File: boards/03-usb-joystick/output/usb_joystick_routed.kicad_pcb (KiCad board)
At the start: 2 copper layers, 80 x 60 mm, 19 parts, among them J1 USB-C, J2 Joystick, SW1 Button, SW2 Button, SW3 Button, SW4 Button, U1 MCU, Y1 16MHz

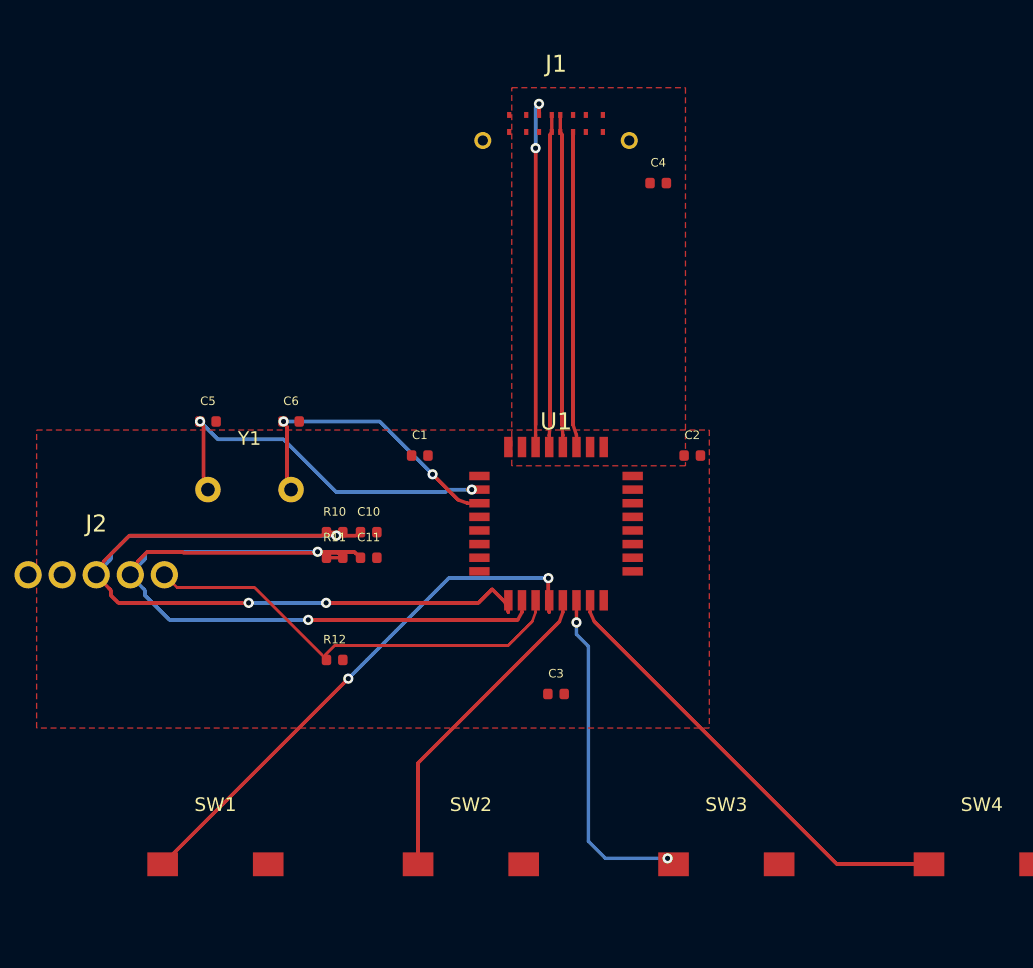
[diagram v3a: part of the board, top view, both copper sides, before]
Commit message: fix(router): grid re-marking after mutating optimizer passes (closes #3507) (#3510)
* fix(router): grid re-marking after mutating optimizer/nudge passes (#3507)

Post-route passes mutated route geometry without re-marking the routing
grid, so their own collision checking and every downstream grid consumer
(targeted repair re-routes, future nets) ran against stale copper:

- RoutingGrid.resync_route_occupancy: explicit resync API taking
  (stale, current) pairs -- unmarks pre-mutation cells (Python + C++
  mirror), swaps grid.routes bookkeeping, rebuilds both R-trees
  wholesale (in-place mutation invalidates id/envelope-keyed entries),
  re-marks all routes of affected nets, invalidates the C++
  stored-route snapshot.  Geometry-unchanged pairs are skipped
  (incremental unmark-old/mark-new perf shape).
- Route.copy_geometry: field-level geometry snapshots for in-place
  mutating passes.
- optimize_routes_grid_synced: grid-transactional optimizer loop
  (unmark old / mark new per mutated route) used by all four kct-route
  call sites and the board 06 recipe.
- drc_verify_and_nudge: snapshots geometry at entry and resyncs the
  grid on every exit path (including exceptions).
- enforce_connectivity_invariant: revert path now resyncs the grid
  with the restored pre-phase routes.
- boards/03: --raw dropped from the production recipe (and the pinned
  baseline-test invocation) -- the grid-transactional optimize retires
  the deterministic XTAL1/XTAL2 clearance_segment_via merge violation
  (closes-#3454 evidence: 13/13 nets + 0 DRC at jlcpcb-tier1 with the
  optimizer ON, seed 42, sidecar-aware check).

Co-Authored-By: Claude Opus 4.7 <noreply@anthropic.com>

* chore(boards): refresh board 03/06 artifacts under grid-synced passes; tighten board 06 floor 33 -> 20 (#3507)

Board 06 (seed 42, PYTHONHASHSEED=0): the 17-error USB3_RX1+/RX1-
overlap cluster (7 diffpair_clearance_intra + 10 clearance_segment_via)
is RETIRED -- the grid-transactional optimizer/nudge passes neve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
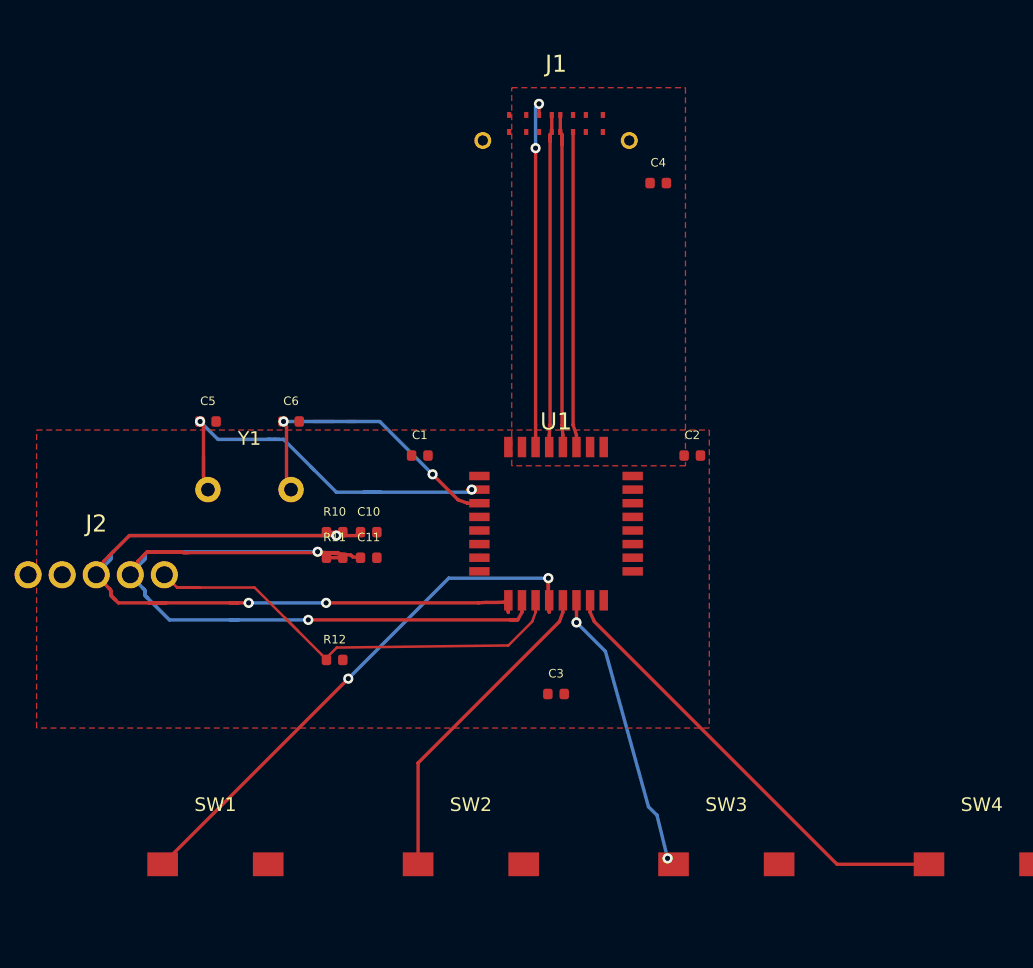
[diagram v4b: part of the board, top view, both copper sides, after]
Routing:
- net BTN3: track 20.0 -> 17.0 mm
- net JOY_X: track 59.2 -> 58.6 mm

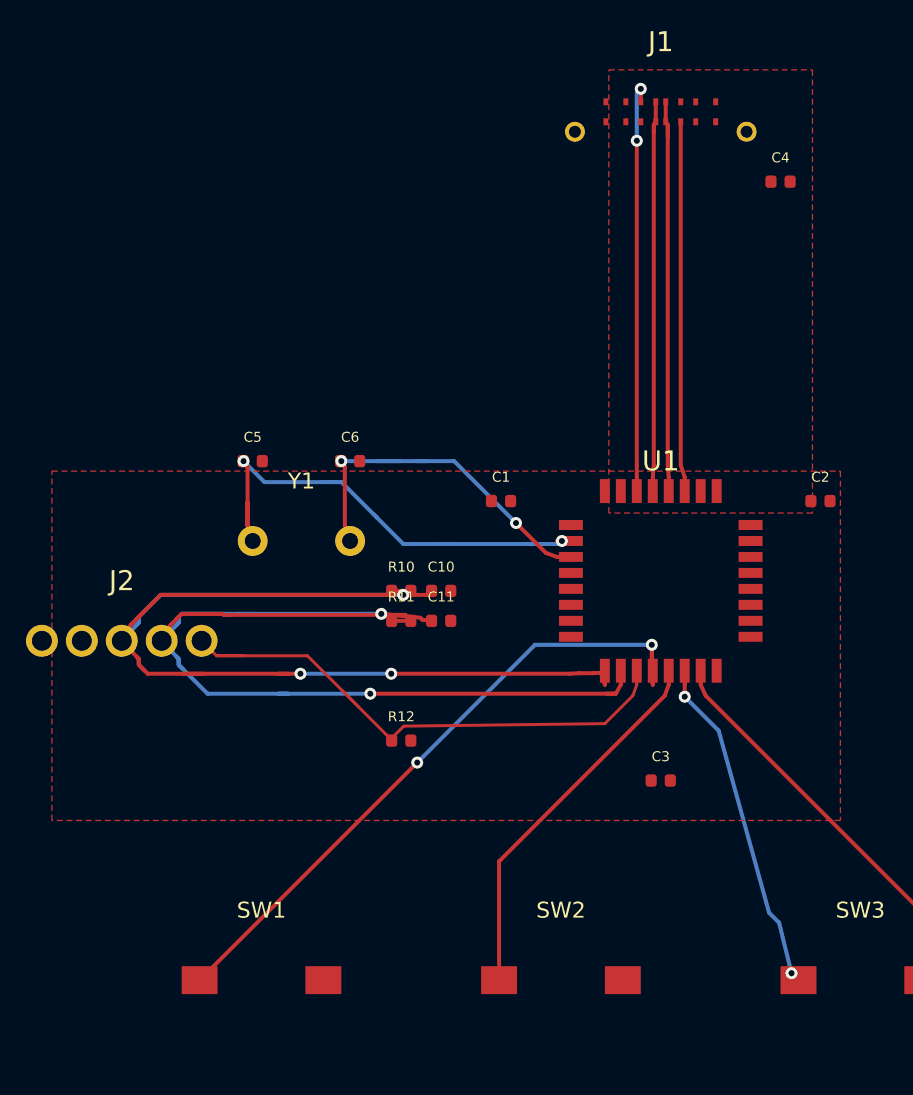
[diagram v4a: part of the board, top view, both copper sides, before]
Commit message: fix(router): 45° quantization in post-route mutation passes (closes #3532)
204/4519 segments on softstart's committed routed artifact sat 0.8-22.5°
off the 0/45/90/135 set; every fleet board carried the same class
(board 07: 297/909). Attribution: 127 pad-tail emissions (the C++
reconstruct_path / Python _convert_path_to_route connect the last grid
cell to the exact off-grid pad centre with one skewed segment), 41
step-10c/d repair chain drags (regex endpoint dragging in
generate_design.py), 36 optimizer mutations (pull-tight neighbour
re-aiming, chamfer terminal restoration).

Fixes at source, all sharing the new router/quantize.py helpers
(is_45_aligned / snap_direction_8 / dogleg_points / quantize_pcb_file):

* cpp_backend._convert_result_to_route splits skewed C++ tails into
  exact float64 doglegs (C++ float32 ulp is too coarse for exact legs)
* Python Router._convert_path_to_route emits dogleg pad tails; the
  extend-to-pad branch requires the extended segment to stay aligned
* convert_corners_45 terminal restoration emits doglegs, not skews
* pull_tight_pass declines windows whose neighbours are not parallel
  to the translation direction (the classic H-V-H jog still compresses)
* drc_nudge segment/via chain snaps decline drags that would skew an
  abutting segment off the 45° set
* softstart recipe: step-10c via slides snap to the 8-direction set;
  new step-10e runs quantize_pcb_file before the DRC gate

Committed artifacts repaired in place with the exact-decimal
quantize_pcb_file (dogleg endpoints preserved bit-for-bit, second-leg
uuids deterministic uuid5). Fleet census ratchet in
tests/test_fleet_45_census.py: softstart + boards 01-05 at 0 off-angle;
documented residuals (issue #3535) are 2 corridor chords where both
dogleg variants collide (06/07) and board 07's 55 DDR_DATA_BYTE_0
length-tuning meanders (doglegging breaks the exactly-tuned
match_group_length_skew).

DRC: softstart 0 violations at jlcpcb-tier1 (strict gate; manufacturers
override added 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
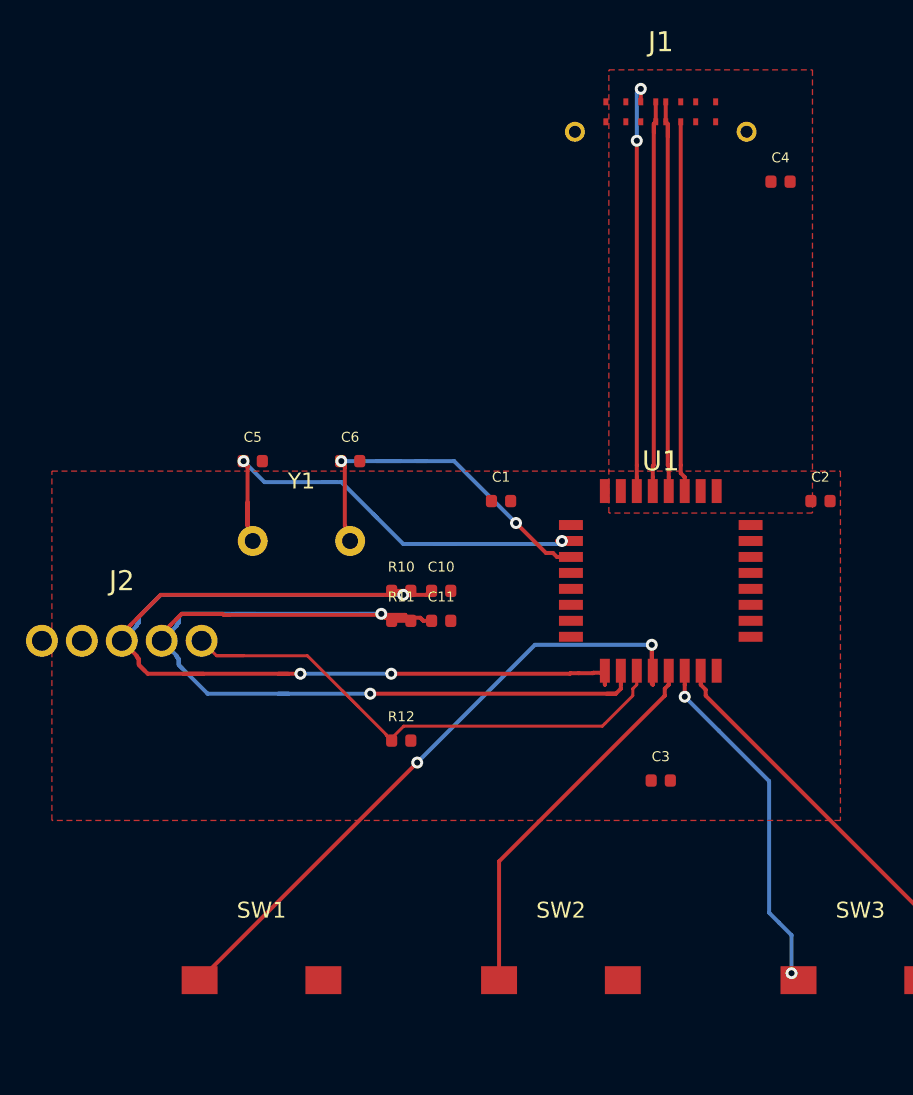
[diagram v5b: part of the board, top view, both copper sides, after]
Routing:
- net BTN3: track 17.0 -> 17.9 mm
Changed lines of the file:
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@@
 	(segment
 		(start 139.65 126.2)
+		(end 139.6 126.25)
+		(width 0.2)
+		(layer "F.Cu")
+		(net 4)
+	)
+	(segment
+		(start 139.6 126.25)
 		(end 139.6 126.8)
 		(width 0.2)
@@
 	(segment
 		(start 139.75 109)
+		(end 139.65 109.1)
+		(width 0.2)
+		(layer "F.Cu")
+		(net 4)
+	)
+	(segment
+		(start 139.65 109.1)
 		(end 139.65 109.15)
 		(width 0.2)
@@
 	(segment
 		(start 140.35 126.2)
+		(end 140.4 126.25)
+		(width 0.2)
+		(layer "F.Cu")
+		(net 5)
+	)
+	(segment
+		(start 140.4 126.25)
 		(end 140.4 126.8)
 		(width 0.2)
@@
 	(segment
 		(start 140.25 109)
+		(end 140.35 109.1)
+		(width 0.2)
+		(layer "F.Cu")
+		(net 5)
+	)
+	(segment
+		(start 140.35 109.1)
 		(end 140.35 109.15)
 		(width 0.2)
@@
 	(segment
 		(start 141.2 126.8)
+		(end 141 126.6)
+		(width 0.2)
+		(layer "F.Cu")
+		(net 7)
+	)
+	(segment
+		(start 141 126.6)
 		(end 141 126.2)
 		(width 0.2)
@@
 	(segment
 		(start 113.45 134.2)
+		(end 113 134.65)
+		(width 0.2)
+		(layer "F.Cu")
+		(net 8)
+	)
+	(segment
+		(start 113 134.65)
 		(end 113 135)
 		(width 0.2)
@@
 	(segment
 		(start 137 136.6)
+		(end 137.2 136.8)
+		(width 0.2)
+		(layer "F.Cu")
+		(net 8)
+	)
+	(segment
+		(start 137.2 136.8)
 		(end 137.2 137.2)
 		(width 0.2)
@@
 	(segment
 		(start 113 135)
+		(end 113.75 135.75)
+		(width 0.2)
+		(layer "F.Cu")
+		(net 8)
+	)
+	(segment
+		(start 113.75 135.75)
 		(end 113.75 135.8)
 		(width 0.2)
@@
 	(segment
 		(start 136.6036 136.6238)
+		(end 136.6274 136.6)
+		(width 0.2)
+		(layer "F.Cu")
+		(net 8)
+	)
+	(segment
+		(start 136.6274 136.6)
 		(end 137 136.6)
 		(width 0.2)
@@
 	(segment
 		(start 135.45 136.65)
+		(end 135.4763 136.6237)
+		(width 0.2)
+		(layer "F.Cu")
+		(net 8)
+	)
+	(segment
+		(start 135.4763 136.6237)
 		(end 135.8964 136.6237)
 		(width 0.2)
@@
 	(segment
 		(start 126.52 132.5)
+		(end 126.32 132.7)
+		(width 0.2)
+		(layer "F.Cu")
+		(net 8)
+	)
+	(segment
+		(start 126.32 132.7)
 		(end 126.25 132.7)
 		(width 0.2)
@@
 	(segment
 		(start 128.25 132.7)
+		(end 128.45 132.5)
+		(width 0.2)
+		(layer "F.Cu")
+		(net 8)
+	)
+	(segment
+		(start 128.45 132.5)
 		(end 128.52 132.5)
 		(width 0.2)
@@
 	(segment
 		(start 113 135)
+		(end 113.75 134.25)
+		(width 0.2)
+		(layer "B.Cu")
+		(net 8)
+	)
+	(segment
+		(start 113.75 134.25)
 		(end 113.75 134.2)
 		(width 0.2)
@@
 	(segment
 		(start 126 133.65)
+		(end 126.1947 133.8447)
+		(width 0.2)
+		(layer "F.Cu")
+		(net 9)
+	)
+	(segment
+		(start 126.1947 133.8447)
 		(end 127.9553 133.8447)
 		(width 0.2)
@@
 	(segment
 		(start 128.0553 133.9447)
+		(end 128.1106 134)
+		(width 0.2)
+		(layer "F.Cu")
+		(net 9)
+	)
+	(segment
+		(start 128.1106 134)
 		(end 128.52 134)
 		(width 0.2)
@@
 	(segment
 		(start 127.48 134)
+		(end 127.2 133.72)
+		(width 0.2)
+		(layer "F.Cu")
+		(net 9)
+	)
+	(segment
+		(start 127.2 133.72)
 		(end 127.2 133.7)
 		(width 0.2)
@@
 	(segment
 		(start 115.45 134.2)
+		(end 115 134.65)
+		(width 0.2)
+		(layer "F.Cu")
+		(net 9)
+	)
+	(segment
+		(start 115 134.65)
 		(end 115 135)
 		(width 0.2)
@@
 	(segment
 		(start 137.75 137.65)
+		(end 138 137.4)
+		(width 0.2)
+		(layer "F.Cu")
+		(net 9)
+	)
+	(segment
+		(start 138 137.4)
 		(end 138 137.2)
 		(width 0.2)
@@
 	(segment
 		(start 115 135)
+		(end 115.75 134.25)
+		(width 0.2)
+		(layer "B.Cu")
+		(net 9)
+	)
+	(segment
+		(start 115.75 134.25)
 		(end 115.75 134.2)
 		(width 0.2)
@@
 	(segment
 		(start 115 135)
+		(end 115.75 135.75)
+		(width 0.2)
+		(layer "B.Cu")
+		(net 9)
+	)
+	(segment
+		(start 115.75 135.75)
 		(end 115.75 135.8)
 		(width 0.2)
@@
 	(segment
 		(start 126.52 140)
+		(end 126.25 139.73)
+		(width 0.15)
+		(layer "F.Cu")
+		(net 10)
+	)
+	(segment
+		(start 126.25 139.73)
 		(end 126.25 139.7)
 		(width 0.15)
@@
 	(segment
 		(start 137.2 139.15)
+		(end 137.075 139.275)
+		(width 0.15)
+		(layer "F.Cu")
+		(net 10)
+	)
+	(segment
+		(start 137.075 139.275)
 		(end 127.125 139.275)
 		(width 0.15)
@@
 	(segment
 		(start 138.8 137.2)
+		(end 138.6 137.4)
+		(width 0.15)
+		(layer "F.Cu")
+		(net 10)
+	)
+	(segment
+		(start 138.6 137.4)
 		(end 138.6 137.75)
 		(width 0.15)
@@
 	(segment
 		(start 126.575 139.825)
+		(end 126.52 139.88)
+		(width 0.15)
+		(layer "F.Cu")
+		(net 10)
+	)
+	(segment
+		(start 126.52 139.88)
 		(end 126.52 140)
 		(width 0.15)
@@
 	(segment
 		(start 139.6 137.2)
+		(end 139.55 137.15)
+		(width 0.2)
+		(layer "F.Cu")
+		(net 11)
+	)
+	(segment
+		(start 139.55 137.15)
 		(end 139.55 136.6)
 		(width 0.2)
@@
 	(segment
 		(start 140.4 137.2)
+		(end 140.2 137.4)
+		(width 0.2)
+		(layer "F.Cu")
+		(net 12)
+	)
+	(segment
+		(start 140.2 137.4)
 		(end 140.2 137.75)
 		(width 0.2)
@@
 	(segment
 		(start 145.9279 149.1221)
+		(end 146.55 149.7442)
+		(width 0.2)
+		(layer "B.Cu")
+		(net 13)
+	)
+	(segment
+		(start 146.55 149.7442)
 		(end 146.55 151.65)
 		(width 0.2)
@@
 	(segment
 		(start 142.9 139.5)
+		(end 145.4279 142.0279)
+		(width 0.2)
+		(layer "B.Cu")
+		(net 13)
+	)
+	(segment
+		(start 145.4279 142.0279)
 		(end 145.4279 148.6221)
 		(width 0.2)
@@
 	(segment
 		(start 142 137.2)
+		(end 142.25 137.45)
+		(width 0.2)
+		(layer "F.Cu")
+		(net 14)
+	)
+	(segment
+		(start 142.25 137.45)
 		(end 142.25 137.75)
 		(width 0.2)
@@
 	(segment
 		(start 119.08 126)
+		(end 119.3 126.22)
+		(width 0.2)
+		(layer "F.Cu")
+		(net 15)
+	)
+	(segment
+		(start 119.3 126.22)
 		(end 119.3 126.3)
 		(width 0.2)
@@
 	(segment
 		(start 119.3 129.25)
+		(end 119.56 129.51)
+		(width 0.2)
+		(layer "F.Cu")
+		(net 15)
+	)
+	(segment
+		(start 119.56 129.51)
 		(end 119.56 130)
 		(width 0.2)
@@
 	(segment
 		(start 123.96 126)
+		(end 124.1734 126.2134)
+		(width 0.2)
+		(layer "F.Cu")
+		(net 16)
+	)
+	(segment
+		(start 124.1734 126.2134)
 		(end 124.1734 126.3)
 		(width 0.2)
@@
 	(segment
 		(start 134.8 130.8)
+		(end 134.6 130.6)
+		(width 0.2)
+		(layer "F.Cu")
+		(net 16)
+	)
+	(segment
+		(start 134.6 130.6)
 		(end 134.25 130.6)
 		(width 0.2)
@@
 	(segment
 		(start 124.1734 129.25)
+		(end 124.44 129.5166)
+		(width 0.2)
+		(layer "F.Cu")
+		(net 16)
+	)
+	(segment
+		(start 124.44 129.5166)
 		(end 124.44 130)
 		(width 0.2)

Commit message: fix(boards/03): re-fill zones against final copper -- clear 4 stale-fill shorts (closes #3551)
The committed board 03 artifact shipped stale GND B.Cu zone fills: 4
BTN3 segments overlapped foreign-net fill copper (up to 1.461mm deep).
`kct zones fill` regenerated the pours against the final trace set
(refill-only -- all 582 segments / 15 vias / 19 footprints are
set-identical to main; zone outlines unchanged). Full `kct check --mfr
jlcpcb-tier1` is now 0 errors, so the grandfathered board-03 entry is
removed from .github/routed-drc-tolerance.yml and the baseline test
ceiling returns to 0. Manufacturing bundle regenerated from the
refilled artifact; BOM/CPL content identical to main (modulo #3529 LF
convention).

Co-Authored-By: Claude Opus 4.7 <noreply@anthropic.com>
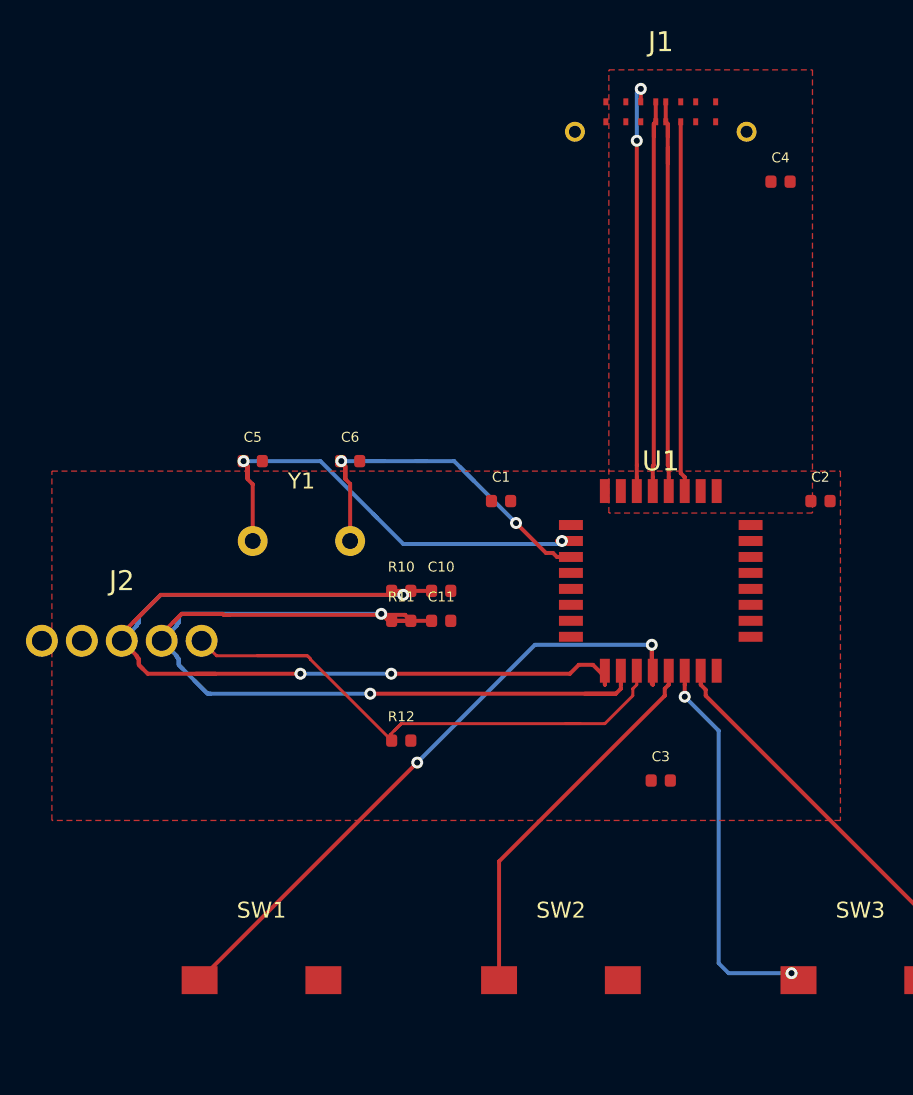
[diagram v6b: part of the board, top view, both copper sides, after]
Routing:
- net BTN3: track 17.9 -> 19.7 mm
